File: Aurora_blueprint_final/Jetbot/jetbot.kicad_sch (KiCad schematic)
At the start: 6 parts, among them J1 Raspberry_Pi_4, J2 Jetson nano, M1 Motor_DC, M2 Motor_DC, U1 BMI160, U2 Flir_LEPTON

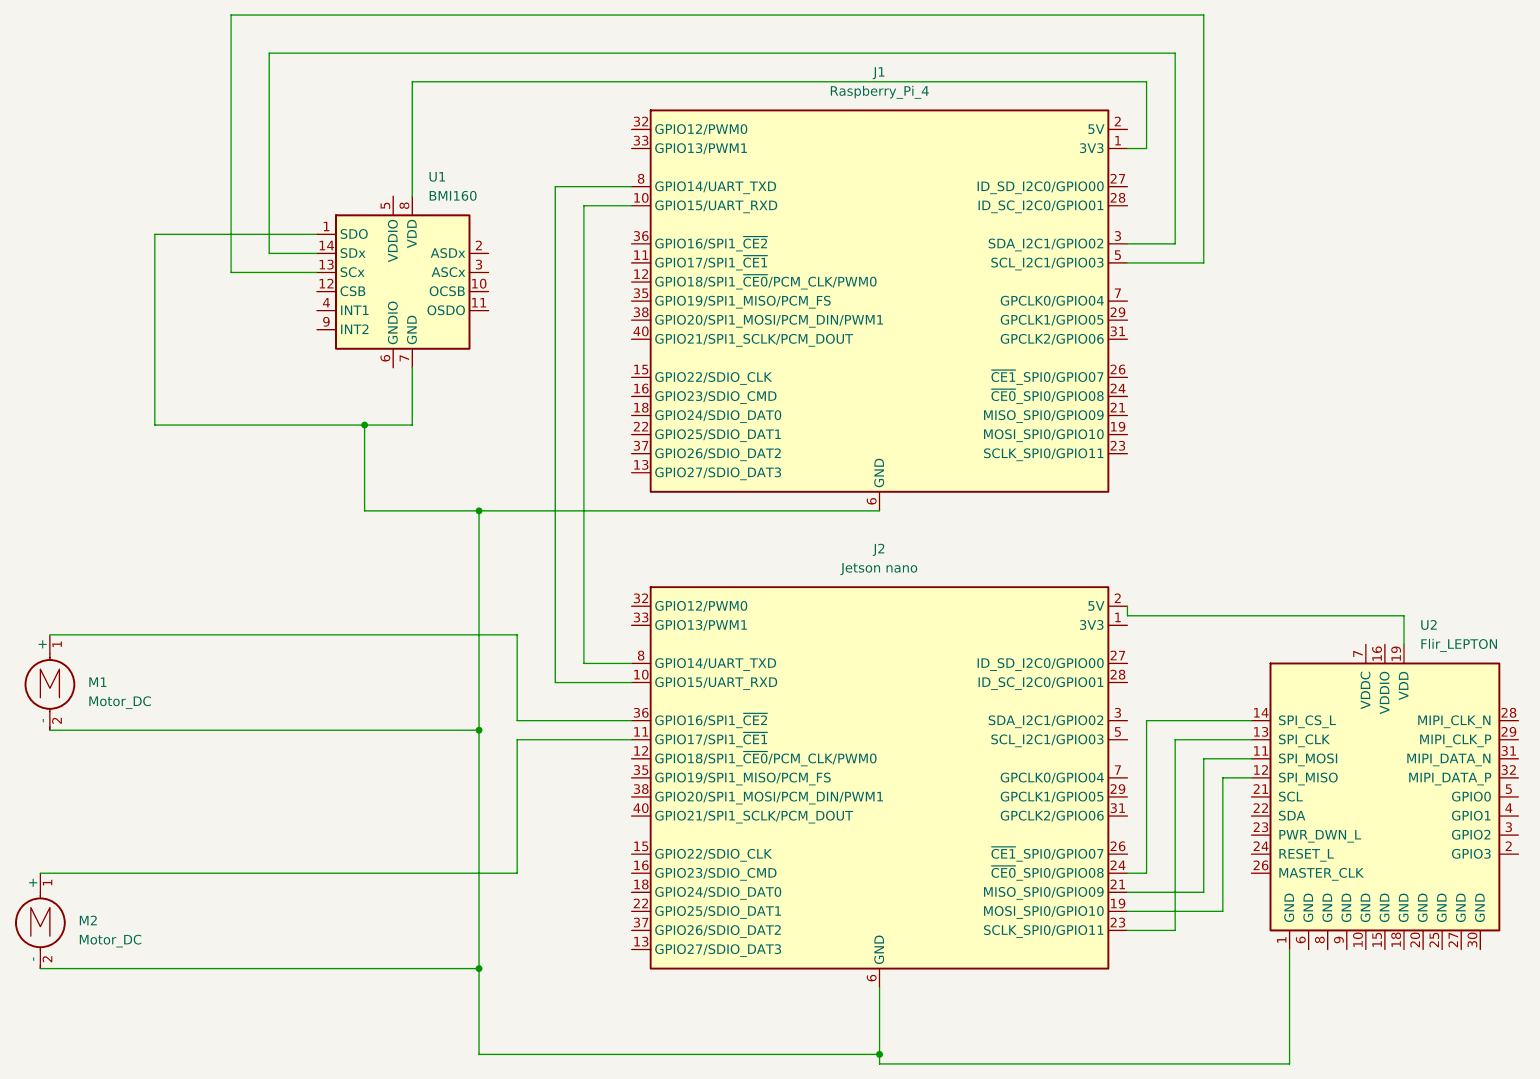
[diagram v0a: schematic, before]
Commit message: moved cam to correct pcb
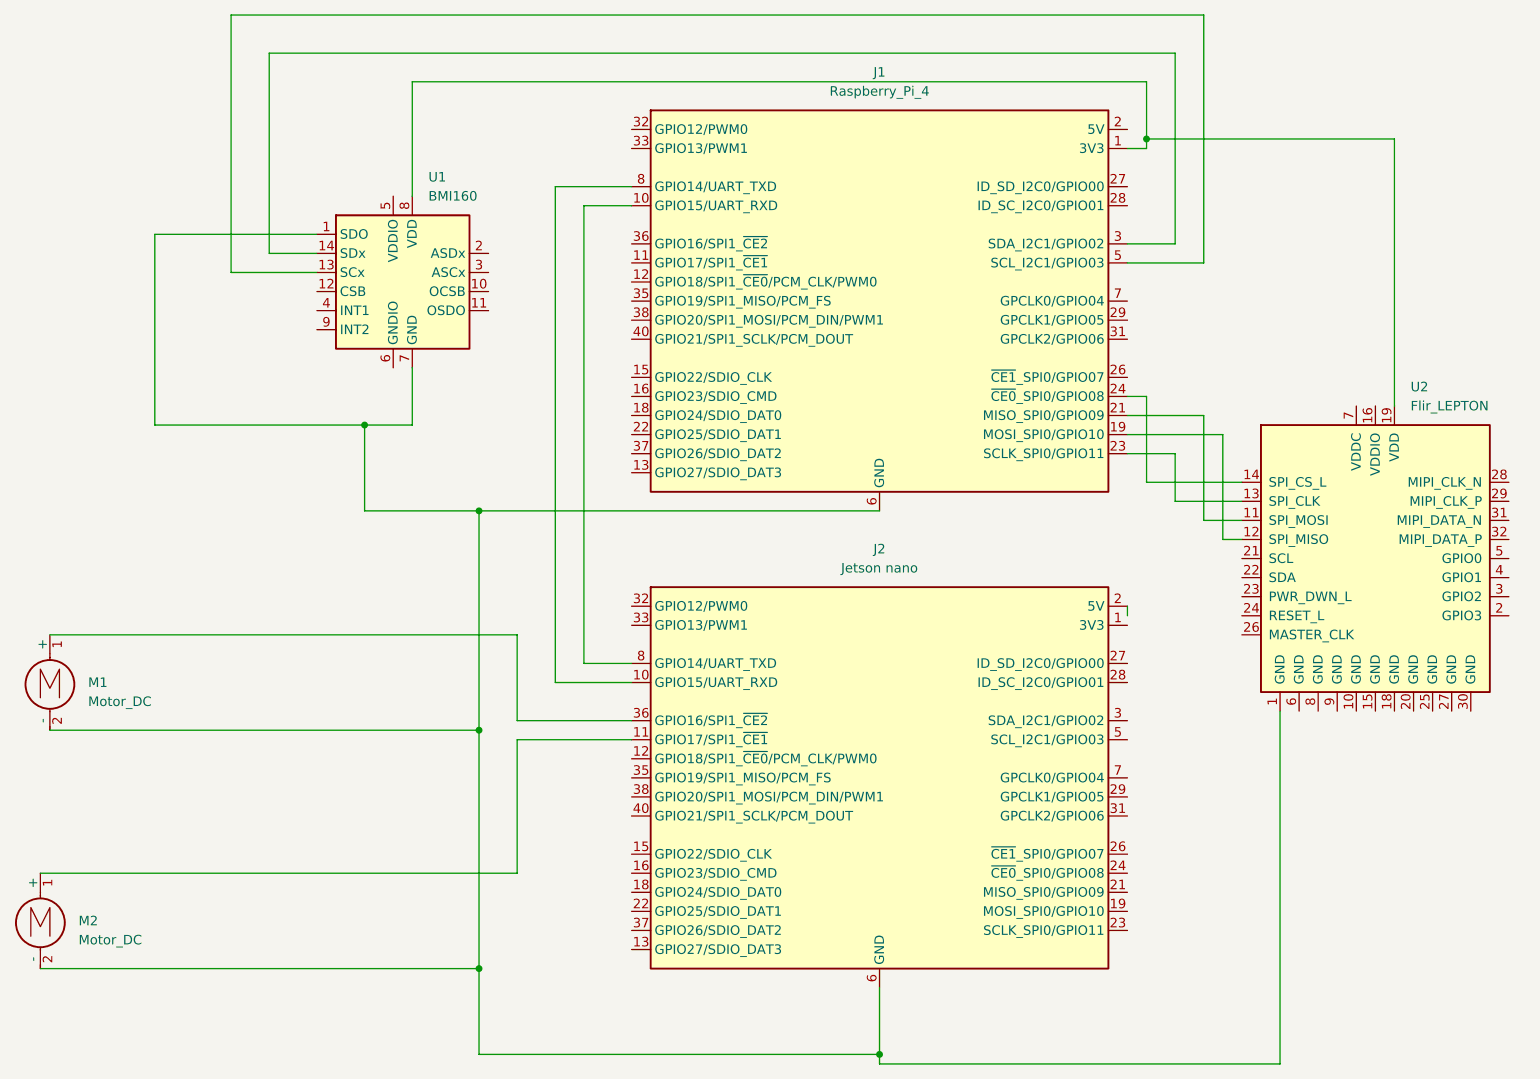
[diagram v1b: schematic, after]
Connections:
- net at J1.1 (3V3), J1.17 (3V3), U1.8 (VDD): now also U2.19 (VDD)
- net at J2.19 (MOSI_SPI0/GPIO10): no longer U2.12 (SPI_MISO)
- net at J2.2 (5V), J2.4 (5V): no longer U2.19 (VDD)
- net at J2.21 (MISO_SPI0/GPIO09): no longer U2.11 (SPI_MOSI)
- net at J2.23 (SCLK_SPI0/GPIO11): no longer U2.13 (SPI_CLK)
- net at J2.24 (~{CE0}_SPI0/GPIO08): no longer U2.14 (SPI_CS_L)
- net at J1.19 (MOSI_SPI0/GPIO10): now also U2.12 (SPI_MISO)
- net at J1.21 (MISO_SPI0/GPIO09): now also U2.11 (SPI_MOSI)
- net at J1.23 (SCLK_SPI0/GPIO11): now also U2.13 (SPI_CLK)
- net at J1.24 (~{CE0}_SPI0/GPIO08): now also U2.14 (SPI_CS_L)
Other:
- moved on the sheet: U2
